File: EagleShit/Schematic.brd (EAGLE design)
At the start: 52.1 x 84.8 mm, 9 parts

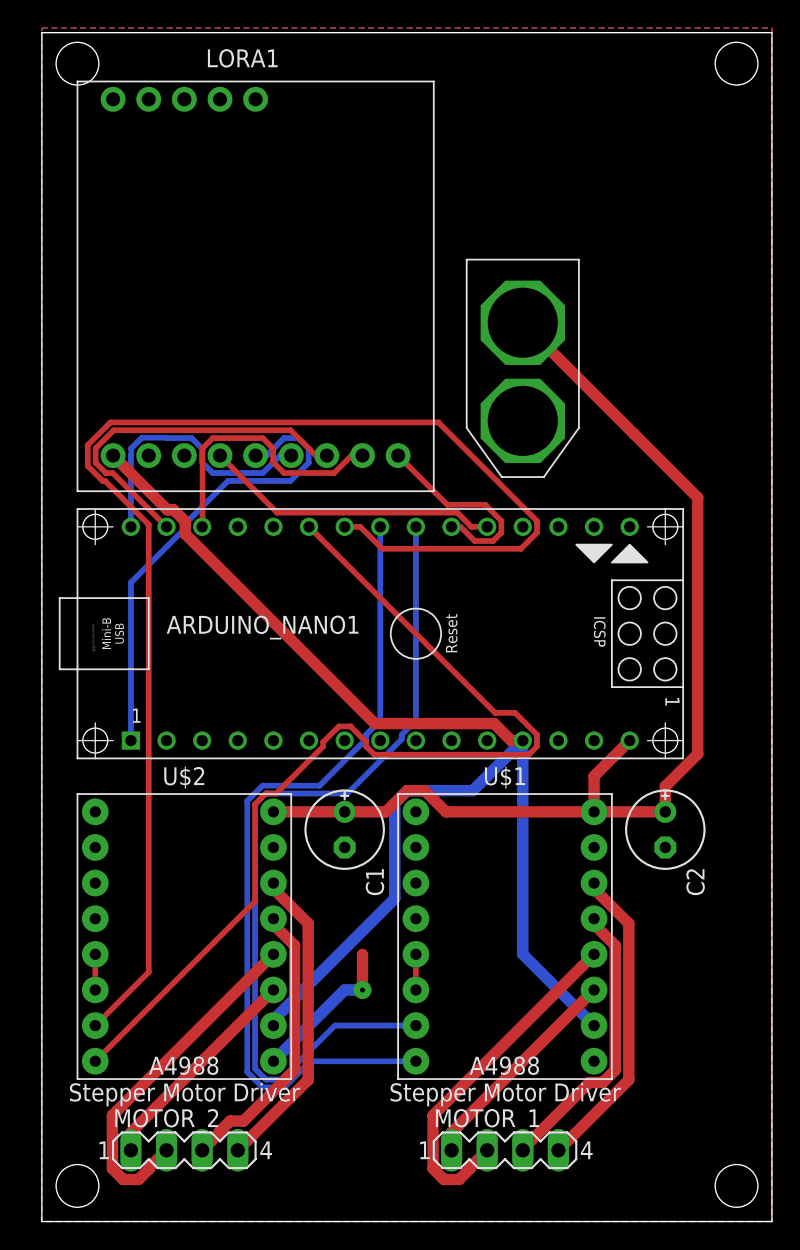
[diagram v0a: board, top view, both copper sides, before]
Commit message: Added Enable Pins
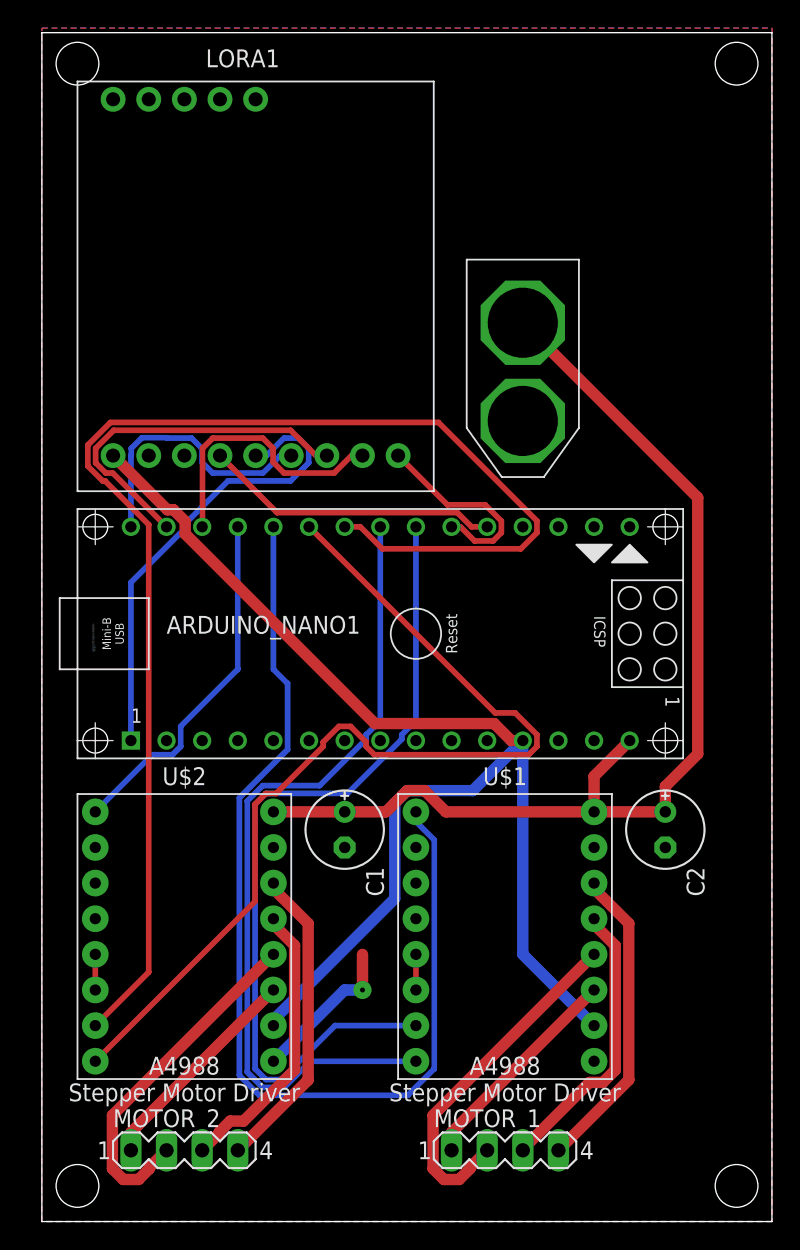
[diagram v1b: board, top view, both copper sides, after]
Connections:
- new net N$12: ARDUINO_NANO1.27, U$2./EN
- new net N$4: ARDUINO_NANO1.26, U$1./EN
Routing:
- net N$4: track 0.00 -> 75.1 mm
- net N$12: track 0.00 -> 25.4 mm
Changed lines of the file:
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@@
 <wire x1="43.18" y1="48.80118125" x2="43.18" y2="46.99" width="0.8128" layer="1"/>
 <wire x1="45.4914" y1="51.11258125" x2="43.18" y2="48.80118125" width="0.8128" layer="1"/>
-<wire x1="33.02" y1="81.86" x2="40.93" y2="73.95" width="0.8128" layer="1"/>
-<wire x1="40.93" y1="73.95" x2="45.4914" y2="69.3886" width="0.8128" layer="1"/>
+<wire x1="33.02" y1="81.86" x2="45.4914" y2="69.3886" width="0.8128" layer="1"/>
 <wire x1="45.4914" y1="69.3886" x2="45.4914" y2="51.11258125" width="0.8128" layer="1"/>
 <wire x1="43.18" y1="46.99" x2="38.1" y2="46.99" width="0.8128" layer="1"/>
@@
 <contactref element="ARDUINO_NANO1" pad="14"/>
 </signal>
+<signal name="N$4">
+<contactref element="ARDUINO_NANO1" pad="26"/>
+<contactref element="U$1" pad="/EN"/>
+<wire x1="15.24" y1="67.31" x2="15.24" y2="57.15" width="0.4064" layer="16"/>
+<wire x1="12.8143" y1="47.994775" x2="12.8143" y2="28.205225" width="0.4064" layer="16"/>
+<wire x1="12.8143" y1="28.205225" x2="14.235225" y2="26.7843" width="0.4064" layer="16"/>
+<wire x1="26.7081" y1="28.6681625" x2="26.7081" y2="44.9918375" width="0.4064" layer="16"/>
+<wire x1="15.24" y1="57.15" x2="16.2496" y2="56.1404" width="0.4064" layer="16"/>
+<wire x1="26.7081" y1="44.9918375" x2="25.4" y2="46.2999375" width="0.4064" layer="16"/>
+<wire x1="25.4" y1="46.2999375" x2="25.4" y2="46.99" width="0.4064" layer="16"/>
+<wire x1="14.235225" y1="26.7843" x2="24.8242375" y2="26.7843" width="0.4064" layer="16"/>
+<wire x1="24.8242375" y1="26.7843" x2="26.7081" y2="28.6681625" width="0.4064" layer="16"/>
+<wire x1="16.2496" y1="56.1404" x2="16.2496" y2="51.430075" width="0.4064" layer="16"/>
+<wire x1="16.2496" y1="51.430075" x2="12.8143" y2="47.994775" width="0.4064" layer="16"/>
+</signal>
+<signal name="N$12">
+<contactref element="ARDUINO_NANO1" pad="27"/>
+<contactref element="U$2" pad="/EN"/>
+<wire x1="12.7" y1="67.31" x2="12.7" y2="57.15" width="0.4064" layer="16"/>
+<wire x1="8.6296" y1="51.65180625" x2="8.03819375" y2="51.0604" width="0.4064" layer="16"/>
+<wire x1="12.7" y1="57.15" x2="8.6296" y2="53.0796" width="0.4064" layer="16"/>
+<wire x1="6.6104" y1="51.0604" x2="2.54" y2="46.99" width="0.4064" layer="16"/>
+<wire x1="8.6296" y1="53.0796" x2="8.6296" y2="51.65180625" width="0.4064" layer="16"/>
+<wire x1="8.03819375" y1="51.0604" x2="6.6104" y2="51.0604" width="0.4064" layer="16"/>
+</signal>
 </signals>
